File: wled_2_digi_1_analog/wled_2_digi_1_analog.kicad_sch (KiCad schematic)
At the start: 49 parts, among them J1 Barrel_Jack_Switch, J2 Screw_Terminal_01x01, J3 Screw_Terminal_01x04, J4 Screw_Terminal_01x04, J5 Screw_Terminal_01x05, Q1 IRLR7843TR(UMW), Q2 AP15P04S, Q3 MMBT4401LT1G, Q4 MMBT4401LT1G, Q5 AP15P04S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

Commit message: Update
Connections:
- net A_CH1: now also ESP32-S3-Board1.17 (IO_11)
- net A_CH2: now also ESP32-S3-Board1.35 (IO_12)
- net A_CH3: now also ESP32-S3-Board1.16 (IO_9)
- net A_CH4: now also ESP32-S3-Board1.11 (IO_5), R16.2; no longer R16.1
- net A_CH5: now also ESP32-S3-Board1.2 (IO_4)
- net ACH3: now reaches J5.3 (Pin_3), Q7.2 (D)
- net at Q8.1 (G), R17.1: now also R16.1; no longer R16.2
- net ACH4: now reaches J5.4 (Pin_4), Q8.2 (D)
- net ACH1: now reaches J5.1 (Pin_1), Q1.2 (D)
- net V_Analog: now reaches FH4.1, J2.1 (Pin_1)
- net ACH5: now reaches J5.5 (Pin_5), Q9.2 (D)
- net ACH2: now reaches J5.2 (Pin_2), Q6.2 (D)
- no-connect marks 26 -> 21
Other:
- moved on the sheet: J2, R16

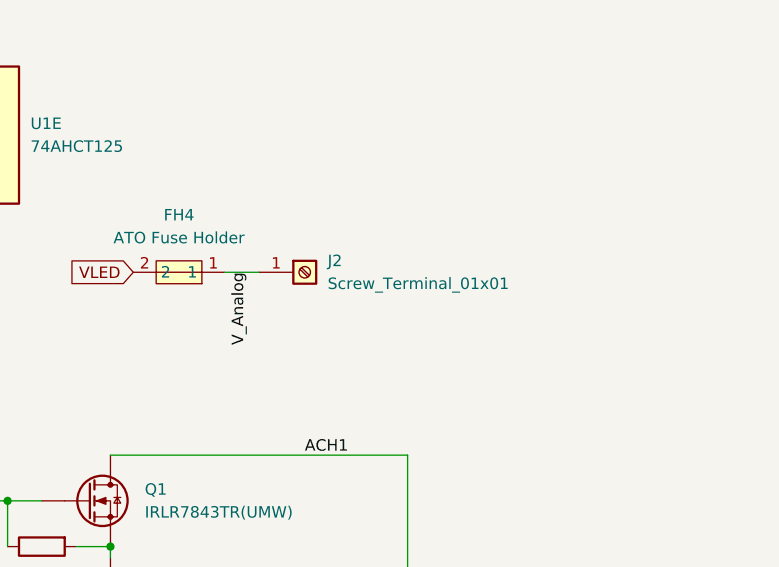
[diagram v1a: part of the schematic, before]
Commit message: Mounting Holes and 2pin connector
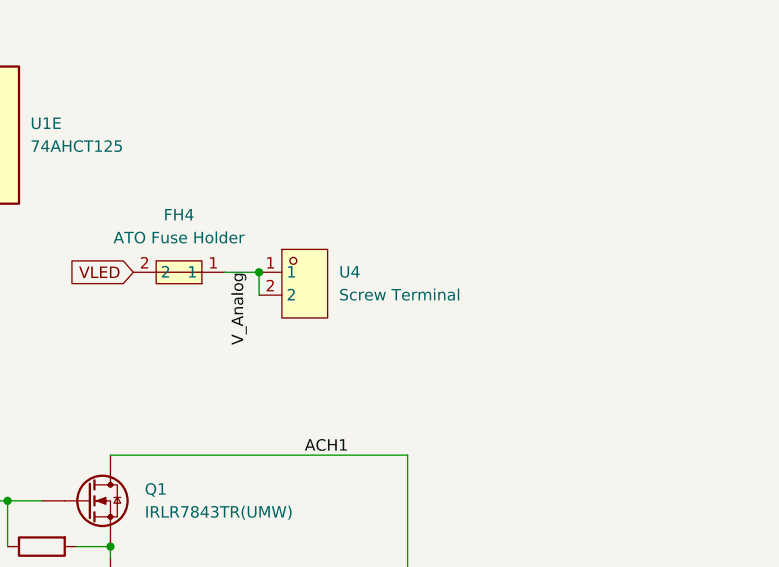
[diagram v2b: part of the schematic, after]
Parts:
- removed J2: Screw_Terminal_01x01, NicosLib:CONN-TH_P5.00_KF301-5.0-1P, symbol Connector:Screw_Terminal_01x01
- added U4: Screw Terminal, easyeda2kicad:CONN-TH_P5.00_KF301-5.0-2P, symbol easyeda2kicad:KF301-5.0-2P
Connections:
- net V_Analog: now also U4.1, U4.2
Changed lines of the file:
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@@
 	)
 	(junction
+		(at 220.98 58.42)
+		(diameter 0)
+		(color 0 0 0 0)
+	)
+	(junction
 		(at 189.23 30.48)
 		(diameter 0)
@@
 	(wire
 		(pts
+			(xy 220.98 58.42) (xy 220.98 60.96)
+		)
+		(stroke
+			(width 0)
+			(type default)
+		)
+	)
+	(wire
+		(pts
 			(xy 111.76 129.54) (xy 114.3 129.54)
 		)
@@
 	)
 	(symbol
+		(lib_id "easyeda2kicad:KF301-5.0-2P")
+		(at 226.06 59.69 0)
+		(unit 1)
+		(body_style 1)
+		(exclude_from_sim no)
+		(in_bom yes)
+		(on_board yes)
+		(in_pos_files yes)
+		(dnp no)
+		(fields_autoplaced yes)
+		(property "Reference" "U4"
+			(at 229.87 58.4199 0)
+			(show_name no)
+			(do_not_autoplace no)
+			(effects
+				(font
+					(size 1.27 1.27)
+				)
+				(justify left)
+			)
+		)
+		(property "Value" "Screw Terminal"
+			(at 229.87 60.9599 0)
+			(show_name no)
+			(do_not_autoplace no)
+			(effects
+				(font
+					(size 1.27 1.27)
+				)
+				(justify left)
+			)
+		)
+		(property "Footprint" "easyeda2kicad:CONN-TH_P5.00_KF301-5.0-2P"
+			(at 226.06 68.58 0)
+			(hide yes)
+			(show_name no)
+			(do_not_autoplace no)
+			(effects
+				(font
+					(size 1.27 1.27)
+				)
+			)
+		)
+		(property "Datasheet" "https://lcsc.com/product-detail/New-Quadratic-Unclassified-Data_Cixi-Kefa-Elec-KF301-5-0-2P_C474881.html"
+			(at 226.06 71.12 0)
+			(hide yes)
+			(show_name no)
+			(do_not_autoplace no)
+			(effects
+				(font
+					(size 1.27 1.27)
+				)
+			)
+		)
+		(property "Description" ""
+			(at 226.06 59.69 0)
+			(hide yes)
+			(show_name no)
+			(do_not_autoplace no)
+			(effects
+				(font
+					(size 1.27 1.27)
+				)
+			)
+		)
+		(property "LCSC Part" "C474881"
+			(at 226.06 73.66 0)
+			(hide yes)
+			(show_name no)
+			(do_not_autoplace no)
+			(effects
+				(font
+					(size 1.27 1.27)
+				)
+			)
+		)
+		(pin "2"
+		)
+		(pin "1"
+		)
+		(instances
+			(project "wled_2_digi_1_analog"
+				(path "/90043e55-bb25-403a-a367-b02d298d6e10"
+					(reference "U4")
+					(unit 1)
+				)
+			)
+		)
+	)
+	(symbol
 		(lib_id "Device:R")
 		(at 119.38 116.84 90)
@@
 					(unit 1)
 				)
-			)
-		)
-	)
-	(symbol
-		(lib_id "Connector:Screw_Terminal_01x01")
-		(at 226.06 58.42 0)
-		(unit 1)
-		(body_style 1)
-		(exclude_from_sim no)
-		(in_bom yes)
-		(on_board yes)
-		(in_pos_files yes)
-		(dnp no)
-		(fields_autoplaced yes)
-		(property "Reference" "J2"
-			(at 228.6 57.1499 0)
-			(show_name no)
-			(do_not_autoplace no)
-			(effects
-				(font
-					(size 1.27 1.27)
-				)
-				(justify left)
-			)
-		)
-		(property "Value" "Screw_Terminal_01x01"
-			(at 228.6 59.6899 0)
-			(show_name no)
-			(do_not_autoplace no)
-			(effects
-				(font
-					(size 1.27 1.27)
-				)
-				(justify left)
-			)
-		)
-		(property "Footprint" "NicosLib:CONN-TH_P5.00_KF301-5.0-1P"
-			(at 226.06 58.42 0)
-			(hide yes)
-			(show_name no)
-			(do_not_autoplace no)
-			(effects
-				(font
-					(size 1.27 1.27)
-				)
-			)
-		)
-		(property "Datasheet" ""
-			(at 226.06 58.42 0)
-			(hide yes)
-			(show_name no)
-			(do_not_autoplace no)
-			(effects
-				(font
-					(size 1.27 1.27)
-				)
-			)
-		)
-		(property "Description" "Generic screw terminal, single row, 01x01, script generated (kicad-library-utils/schlib/autogen/connector/)"
-			(at 226.06 58.42 0)
-			(hide yes)
-			(show_name no)
-			(do_not_autoplace no)
-			(effects
-				(font
-					(size 1.27 1.27)
-				)
-			)
-		)
-		(pin "1"
-		)
-		(instances
-			(project "wled_2_digi_1_analog"
-				(path "/90043e55-bb25-403a-a367-b02d298d6e10"
-					(reference "J2")
-					(unit 1)
-				)

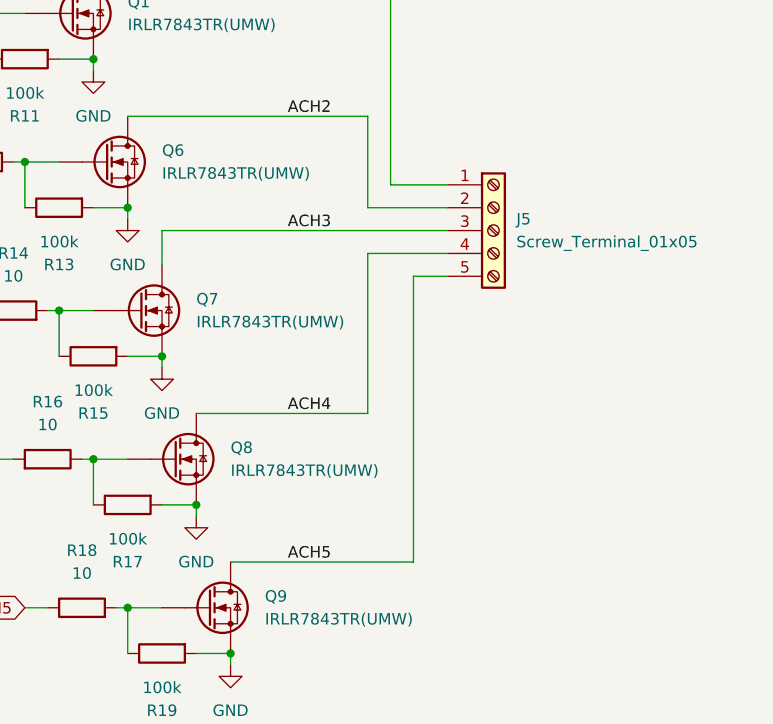
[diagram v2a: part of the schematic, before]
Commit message: Switch 5pin to 2+3ping
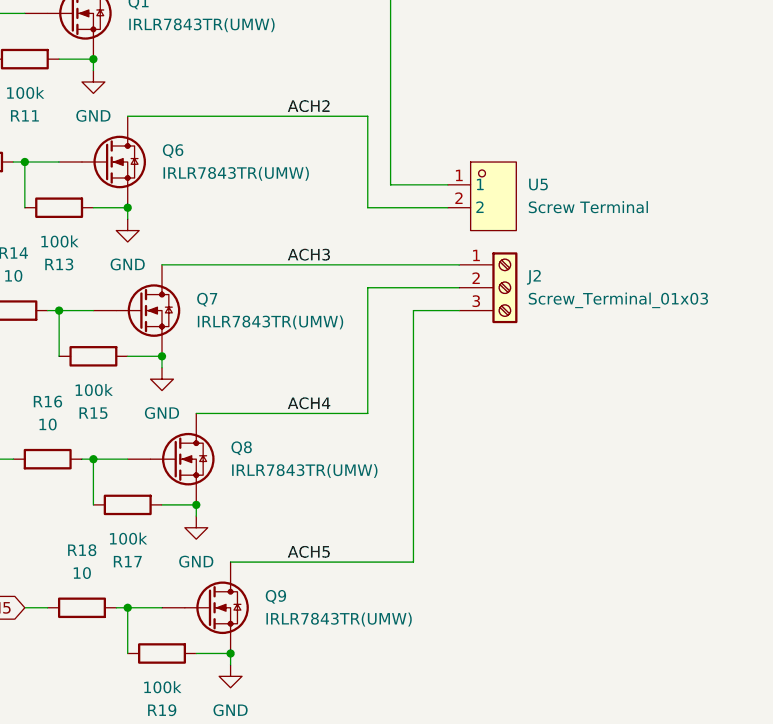
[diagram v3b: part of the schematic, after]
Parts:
- removed J5: Screw_Terminal_01x05, NicosLib:CONN-TH_P5.00_KF301-5.0-5P, symbol Connector:Screw_Terminal_01x05
- added J2: Screw_Terminal_01x03, NicosLib:CONN-TH_P5.00_KF301-5.0-3P, symbol Connector:Screw_Terminal_01x03
- added U5: Screw Terminal, easyeda2kicad:CONN-TH_P5.00_KF301-5.0-2P, symbol easyeda2kicad:KF301-5.0-2P
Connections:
- net ACH1: now also U5.1
- net ACH2: now also U5.2
- net ACH3: now also J2.1 (Pin_1)
- net ACH4: now also J2.2 (Pin_2)
- net ACH5: now also J2.3 (Pin_3)
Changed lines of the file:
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@@
 	(wire
 		(pts
+			(xy 245.11 114.3) (xy 234.95 114.3)
+		)
+		(stroke
+			(width 0)
+			(type default)
+		)
+	)
+	(wire
+		(pts
 			(xy 88.9 160.02) (xy 91.44 160.02)
 		)
@@
 	(wire
 		(pts
+			(xy 212.09 111.76) (xy 245.11 111.76)
+		)
+		(stroke
+			(width 0)
+			(type default)
+		)
+	)
+	(wire
+		(pts
 			(xy 129.54 53.34) (xy 129.54 48.26)
 		)
@@
 	(wire
 		(pts
+			(xy 240.03 144.78) (xy 240.03 116.84)
+		)
+		(stroke
+			(width 0)
+			(type default)
+		)
+	)
+	(wire
+		(pts
 			(xy 100.33 91.44) (xy 100.33 95.25)
 		)
@@
 	(wire
 		(pts
+			(xy 234.95 114.3) (xy 234.95 128.27)
+		)
+		(stroke
+			(width 0)
+			(type default)
+		)
+	)
+	(wire
+		(pts
 			(xy 204.47 138.43) (xy 204.47 133.35)
 		)
@@
 	(wire
 		(pts
-			(xy 243.84 113.03) (xy 240.03 113.03)
-		)
-		(stroke
-			(width 0)
-			(type default)
-		)
-	)
-	(wire
-		(pts
 			(xy 208.28 106.68) (xy 208.28 105.41)
 		)
@@
 	(wire
 		(pts
-			(xy 243.84 107.95) (xy 212.09 107.95)
+			(xy 86.36 53.34) (xy 86.36 55.88)
 		)
 		(stroke
@@
 	(wire
 		(pts
-			(xy 86.36 53.34) (xy 86.36 55.88)
+			(xy 153.67 55.88) (xy 158.75 55.88)
 		)
 		(stroke
@@
 	(wire
 		(pts
-			(xy 153.67 55.88) (xy 158.75 55.88)
+			(xy 123.19 119.38) (xy 137.16 119.38)
 		)
 		(stroke
@@
 	(wire
 		(pts
-			(xy 123.19 119.38) (xy 137.16 119.38)
+			(xy 31.75 24.13) (xy 39.37 24.13)
 		)
 		(stroke
@@
 	(wire
 		(pts
-			(xy 31.75 24.13) (xy 39.37 24.13)
+			(xy 110.49 102.87) (xy 113.03 102.87)
 		)
 		(stroke
@@
 	(wire
 		(pts
-			(xy 110.49 102.87) (xy 113.03 102.87)
+			(xy 177.8 38.1) (xy 177.8 30.48)
 		)
 		(stroke
@@
 	(wire
 		(pts
-			(xy 177.8 38.1) (xy 177.8 30.48)
+			(xy 240.03 116.84) (xy 245.11 116.84)
 		)
 		(stroke
@@
 	(wire
 		(pts
-			(xy 234.95 110.49) (xy 243.84 110.49)
-		)
-		(stroke
-			(width 0)
-			(type default)
-		)
-	)
-	(wire
-		(pts
 			(xy 93.98 66.04) (xy 90.17 66.04)
 		)
@@
 	(wire
 		(pts
-			(xy 212.09 107.95) (xy 212.09 111.76)
-		)
-		(stroke
-			(width 0)
-			(type default)
-		)
-	)
-	(wire
-		(pts
 			(xy 34.29 29.21) (xy 39.37 29.21)
 		)
@@
 	(wire
 		(pts
-			(xy 234.95 128.27) (xy 234.95 110.49)
-		)
-		(stroke
-			(width 0)
-			(type default)
-		)
-	)
-	(wire
-		(pts
 			(xy 237.49 78.74) (xy 204.47 78.74)
 		)
@@
 		)
 	)
-	(wire
-		(pts
-			(xy 240.03 113.03) (xy 240.03 144.78)
-		)
-		(stroke
-			(width 0)
-			(type default)
-		)
-	)
 	(label "VLED_1_Fused"
 		(at 78.74 152.4 0)
@@
 	)
 	(label "ACH3"
-		(at 226.06 107.95 0)
+		(at 226.06 111.76 0)
 		(effects
 			(font
@@
 	)
 	(symbol
+		(lib_id "Connector:Screw_Terminal_01x03")
+		(at 250.19 114.3 0)
+		(unit 1)
+		(body_style 1)
+		(exclude_from_sim no)
+		(in_bom yes)
+		(on_board yes)
+		(in_pos_files yes)
+		(dnp no)
+		(fields_autoplaced yes)
+		(property "Reference" "J2"
+			(at 252.73 113.0299 0)
+			(show_name no)
+			(do_not_autoplace no)
+			(effects
+				(font
+					(size 1.27 1.27)
+				)
+				(justify left)
+			)
+		)
+		(property "Value" "Screw_Terminal_01x03"
+			(at 252.73 115.5699 0)
+			(show_name no)
+			(do_not_autoplace no)
+			(effects
+				(font
+					(size 1.27 1.27)
+				)
+				(justify left)
+			)
+		)
+		(property "Footprint" "NicosLib:CONN-TH_P5.00_KF301-5.0-3P"
+			(at 250.19 114.3 0)
+			(hide yes)
+			(show_name no)
+			(do_not_autoplace no)
+			(effects
+				(font
+					(size 1.27 1.27)
+				)
+			)
+		)
+		(property "Datasheet" ""
+			(at 250.19 114.3 0)
+			(hide yes)
+			(show_name no)
+			(do_not_autoplace no)
+			(effects
+				(font
+					(size 1.27 1.27)
+				)
+			)
+		)
+		(property "Description" "Generic screw terminal, single row, 01x03, script generated (kicad-library-utils/schlib/autogen/connector/)"
+			(at 250.19 114.3 0)
+			(hide yes)
+			(show_name no)
+			(do_not_autoplace no)
+			(effects
+				(font
+					(size 1.27 1.27)
+				)
+			)
+		)
+		(pin "3"
+		)
+		(pin "2"
+		)
+		(pin "1"
+		)
+		(instances
+			(project "wled_2_digi_1_analog"
+				(path "/90043e55-bb25-403a-a367-b02d298d6e10"
+					(reference "J2")
+					(unit 1)
+				)
+			)
+		)
+	)
+	(symbol
 		(lib_id "power:GND")
 		(at 66.04 24.13 90)
@@
 	(symbol
 		(lib_id "easyeda2kicad:KF301-5.0-2P")
+		(at 248.92 104.14 0)
+		(unit 1)
+		(body_style 1)
+		(exclude_from_sim no)
+		(in_bom yes)
+		(on_board yes)
+		(in_pos_files yes)
+		(dnp no)
+		(fields_autoplaced yes)
+		(property "Reference" "U5"
+			(at 252.73 102.8699 0)
+			(show_name no)
+			(do_not_autoplace no)
+			(effects
+				(font
+					(size 1.27 1.27)
+				)
+				(justify left)
+			)
+		)
+		(property "Value" "Screw Terminal"
+			(at 252.73 105.4099 0)
+			(show_name no)
+			(do_not_autoplace no)
+			(effects
+				(font
+					(size 1.27 1.27)
+				)
+				(justify left)
+			)
+		)
+		(property "Footprint" "easyeda2kicad:CONN-TH_P5.00_KF301-5.0-2P"
+			(at 248.92 113.03 0)
+			(hide yes)
+			(show_name no)
+			(do_not_autoplace no)
+			(effects
+				(font
+					(size 1.27 1.27)
+				)
+			)
+		)
+		(property "Datasheet" "https://lcsc.com/product-detail/New-Quadratic-Unclassified-Data_Cixi-Kefa-Elec-KF301-5-0-2P_C474881.html"
+			(at 248.92 115.57 0)
+			(hide yes)
+			(show_name no)
+			(do_not_autoplace no)
+			(effects
+				(font
+					(size 1.27 1.27)
+				)
+			)
+		)
+		(property "Description" ""
+			(at 248.92 104.14 0)
+			(hide yes)
+			(show_name no)
+			(do_not_autoplace no)
+			(effects
+				(font
+					(size 1.27 1.27)
+				)
+			)
+		)
+		(property "LCSC Part" "C474881"
+			(at 248.92 118.11 0)
+			(hide yes)
+			(show_name no)
+			(do_not_autoplace no)
+			(effects
+				(font
+					(size 1.27 1.27)
+				)
+			)
+		)
+		(pin "2"
+		)
+		(pin "1"
+		)
+		(instances
+			(project "wled_2_digi_1_analog"
+				(path "/90043e55-bb25-403a-a367-b02d298d6e10"
+					(reference "U5")
+					(unit 1)
+				)
+			)
+		)
+	)
+	(symbol
+		(lib_id "easyeda2kicad:KF301-5.0-2P")
 		(at 226.06 59.69 0)
 		(unit 1)
@@
 					(unit 1)
 				)
-			)
-		)
-	)
-	(symbol
-		(lib_id "Connector:Screw_Terminal_01x05")
-		(at 248.92 107.95 0)
-		(unit 1)
-		(body_style 1)
-		(exclude_from_sim no)
-		(in_bom yes)
-		(on_board yes)
-		(in_pos_files yes)
-		(dnp no)
-		(fields_autoplaced yes)
-		(property "Reference" "J5"
-			(at 251.46 106.6799 0)
-			(show_name no)
-			(do_not_autoplace no)
-			(effects
-				(font
-					(size 1.27 1.27)
-				)
-				(justify left)
-			)
-		)
-		(property "Value" "Screw_Terminal_01x05"
-			(at 251.46 109.2199 0)
-			(show_name no)
-			(do_not_autoplace no)
-			(effects
-				(font
-					(size 1.27 1.27)
-				)
-				(justify left)
-			)
-		)
-		(property "Footprint" "NicosLib:CONN-TH_P5.00_KF301-5.0-5P"
-			(at 248.92 107.95 0)
-			(hide yes)
-			(show_name no)
-			(do_not_autoplace no)
-			(effects
-				(font
-					(size 1.27 1.27)
-				)
-			)
-		)
-		(property "Datasheet" ""
-			(at 248.92 107.95 0)
-			(hide yes)
-			(show_name no)
-			(do_not_autoplace no)
-			(effects
-				(font
-					(size 1.27 1.27)
-				)
-			)
-		)
-		(property "Description" "Generic screw terminal, single row, 01x05, script generated (kicad-library-utils/schlib/autogen/connector/)"
-			(at 248.92 107.95 0)
-			(hide yes)
-			(show_name no)
-			(do_not_autoplace no)
-			(effects
-				(font
-					(size 1.27 1.27)
-				)
-			)
-		)
-		(pin "5"
-		)
-		(pin "2"
-		)
-		(pin "4"
-		)
-		(pin "3"
-		)
-		(pin "1"
-		)
-		(instances
-			(project "wled_2_digi_1_analog"
-				(path "/90043e55-bb25-403a-a367-b02d298d6e10"
-					(reference "J5")
-					(unit 1)
-				)
